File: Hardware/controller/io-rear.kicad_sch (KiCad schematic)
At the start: 7 parts

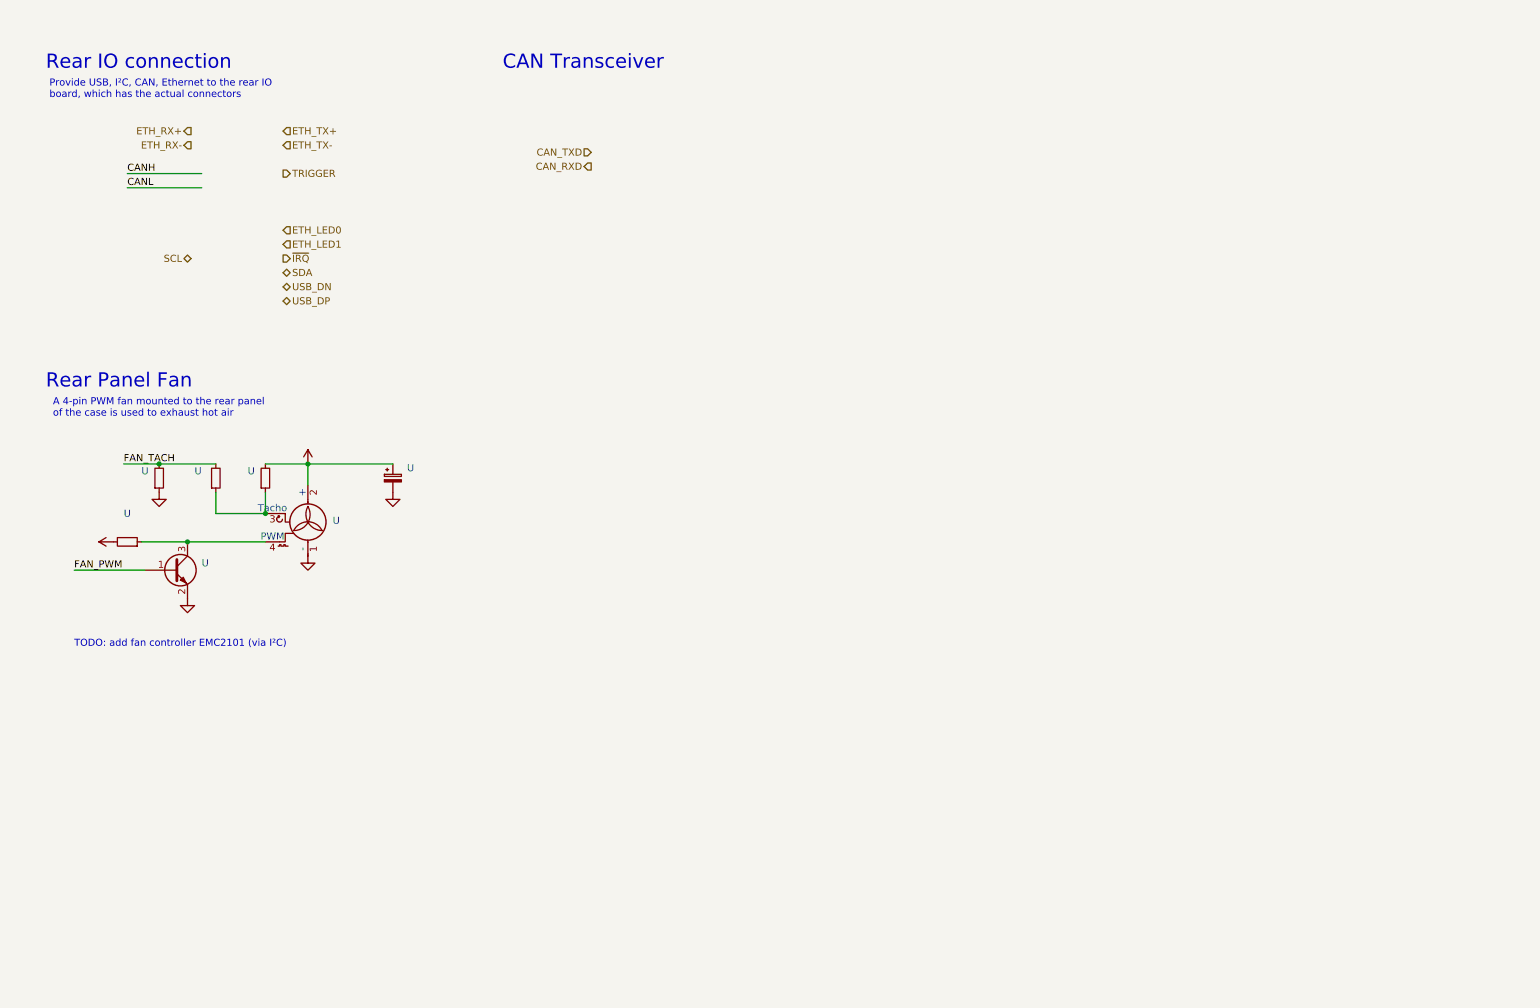
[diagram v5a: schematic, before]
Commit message: More reworking of the controller and friends
- Add more rear IO to the controller, in this case finishing positioning
  of the Ethernet jack, and adding a suitable right angle USB B jack
  (USB C is preferrable but there's basically no jacks that are
  sufficiently long)

- Mostly finish power section on controller (save for the enable input
  for our +3V3 rail; it'll be slaved off the SoM +3V3 rail)

- Minor tweaks to pinout of FFC connector on front panel

- Update cutout shape of analog board

- Fixed a few footprints metadata

- Add footprints for further rear panel IO
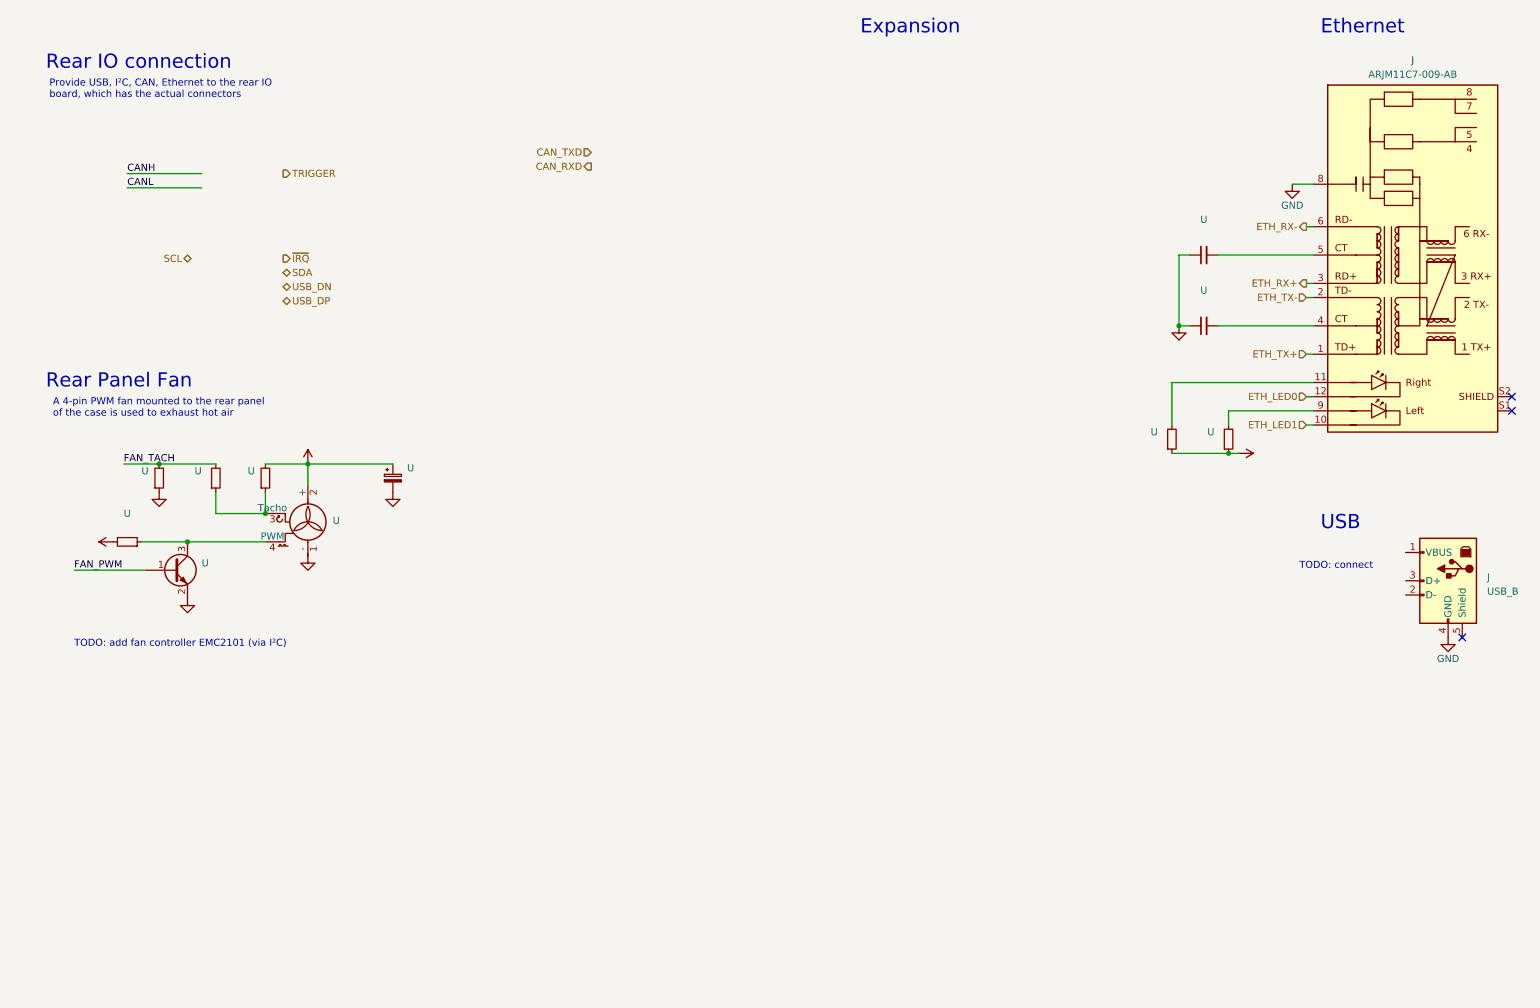
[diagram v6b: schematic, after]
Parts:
- added J: USB_B, symbol Connector:USB_B
- added J: ARJM11C7-009-AB, programmable-load:Abracon-ARJM11C7, symbol programmable-load:ARJM11C7-009-AB
- added U (x2): (no value), symbol Device:R_Small
- added U (x2): (no value), symbol Device:C_Small
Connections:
- net ETH_LED0: now also J.12 (LLED-)
- net ETH_LED1: now also J.10 (RLED-)
- net ETH_RX+: now also J.3 (RD+)
- net ETH_RX-: now also J.6 (RD-)
- net ETH_TX+: now also J.1 (TD+)
- net ETH_TX-: now also J.2 (TD-)
- net GND: now also J.4 (GND), J.8, U.1, U.1
- new net: J.9 (RLED+), U.2
- new net: J.11 (LLED+), U.2
- new net: J.5 (CT), U.2
- new net: J.4 (CT), U.2
- new net +3V3: U.1, U.1
- no-connect marks 0 -> 3
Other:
- note added: "Ethernet"
- note added: "Expansion"
- note added: "TODO: connect"
- note added: "USB"
- note removed: "CAN Transceiver"

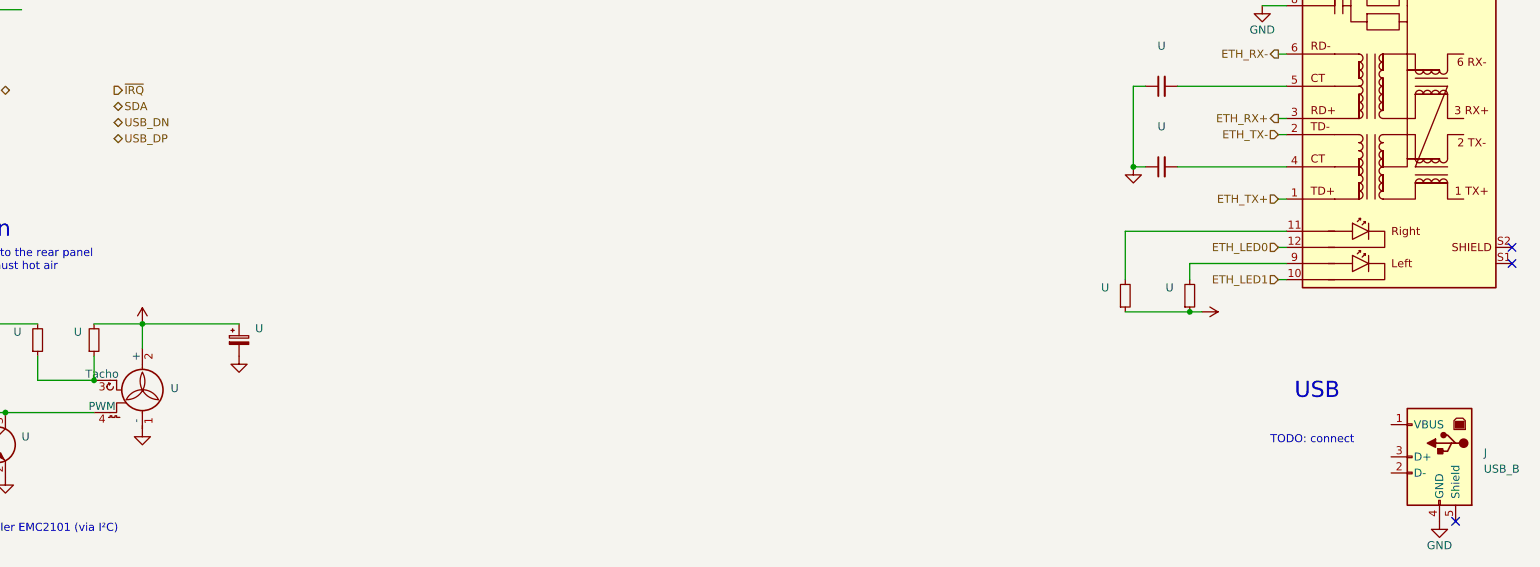
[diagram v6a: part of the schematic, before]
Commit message: More controller power supply work
- Added a voltage supervisor on the SoM's +3V3 rail, which disables our
  +3V3 switching regulator until the SoM rail has come up to a
  reasonable voltage. This avoids the +3V3 rail being powered, and back
  powering stuff on the SoM through ESD diodes.

  There's also a resistor (R204) that may or may not be needed to hold
  the regulator disabled until the power supervisor does its thing; this
  needs to be investigated

- Added ESD protection for USB device jack

- Tweaks to footprint for ARJM11C7 Ethernet jack, to fix DRC errors with
  the LED pads and the mechanical retention thingies
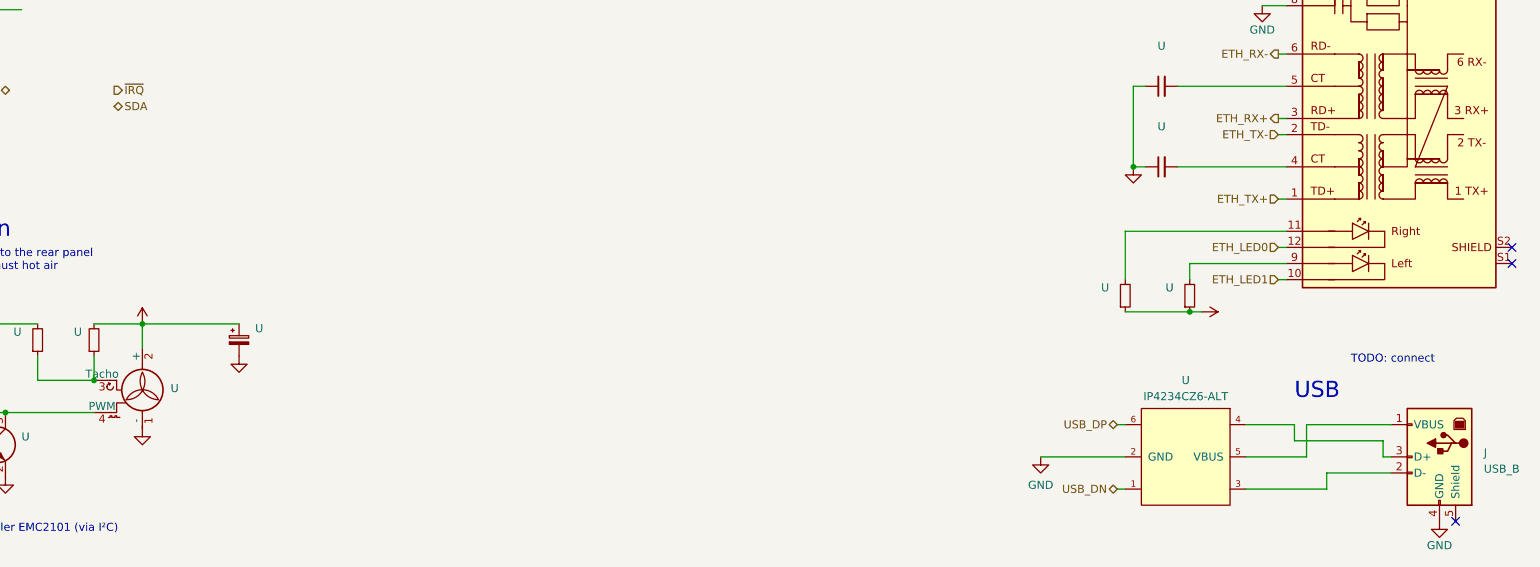
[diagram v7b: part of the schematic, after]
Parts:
- added U: IP4234CZ6-ALT, Package_SO:TSOP-6_1.65x3.05mm_P0.95mm, symbol programmable-load:IP4234CZ6-ALT
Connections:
- net GND: now also U.2 (GND)
- net USB_DN: now also U.1
- net USB_DP: now also U.6
- net at J.1 (VBUS): now also U.5 (VBUS)
- net at J.2 (D-): now also U.3
- net at J.3 (D+): now also U.4
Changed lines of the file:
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@@
+    (stroke (width 0) (type default))
+  )
+  (wire (pts (xy 219.71 121.92) (xy 220.98 121.92))
+    (stroke (width 0) (type default))
+  )
+  (wire (pts (xy 261.62 114.3) (xy 261.62 116.84))
     (stroke (width 0) (type default))
   )
@@
     (stroke (width 0) (type default))
   )
+  (wire (pts (xy 247.65 114.3) (xy 247.65 111.76))
+    (stroke (width 0) (type default))
+  )
   (wire (pts (xy 245.11 66.04) (xy 246.38 66.04))
     (stroke (width 0) (type default))
@@
     (stroke (width 0) (type default))
   )
+  (wire (pts (xy 249.555 111.76) (xy 262.89 111.76))
+    (stroke (width 0) (type default))
+  )
   (wire (pts (xy 49.53 104.775) (xy 49.53 100.965))
     (stroke (width 0) (type default))
   )
+  (wire (pts (xy 219.71 111.76) (xy 220.98 111.76))
+    (stroke (width 0) (type default))
+  )
   (wire (pts (xy 245.11 83.82) (xy 246.38 83.82))
     (stroke (width 0) (type default))
   )
+  (wire (pts (xy 207.645 116.84) (xy 220.98 116.84))
+    (stroke (width 0) (type default))
+  )
+  (wire (pts (xy 252.73 119.38) (xy 252.73 121.92))
+    (stroke (width 0) (type default))
+  )
   (wire (pts (xy 231.14 93.98) (xy 233.045 93.98))
     (stroke (width 0) (type default))
@@
     (stroke (width 0) (type default))
   )
+  (wire (pts (xy 247.65 111.76) (xy 240.03 111.76))
+    (stroke (width 0) (type default))
+  )
+  (wire (pts (xy 247.65 114.3) (xy 261.62 114.3))
+    (stroke (width 0) (type default))
+  )
   (wire (pts (xy 231.14 86.36) (xy 231.14 88.9))
     (stroke (width 0) (type default))
@@
     (stroke (width 0) (type default))
   )
+  (wire (pts (xy 262.89 119.38) (xy 252.73 119.38))
+    (stroke (width 0) (type default))
+  )
+  (wire (pts (xy 262.89 116.84) (xy 261.62 116.84))
+    (stroke (width 0) (type default))
+  )
   (wire (pts (xy 246.38 81.28) (xy 220.98 81.28))
     (stroke (width 0) (type default))
@@
     (stroke (width 0) (type default))
   )
+  (wire (pts (xy 252.73 121.92) (xy 240.03 121.92))
+    (stroke (width 0) (type default))
+  )
   (wire (pts (xy 242.57 45.72) (xy 246.38 45.72))
     (stroke (width 0) (type default))
@@
     (stroke (width 0) (type default))
   )
+  (wire (pts (xy 240.03 116.84) (xy 249.555 116.84))
+    (stroke (width 0) (type default))
+  )
   (wire (pts (xy 58.42 95.885) (xy 66.04 95.885))
     (stroke (width 0) (type default))
@@
   )
   (wire (pts (xy 222.25 58.42) (xy 224.155 58.42))
+    (stroke (width 0) (type default))
+  )
+  (wire (pts (xy 249.555 111.76) (xy 249.555 116.84))
     (stroke (width 0) (type default))
   )
@@
     (effects (font (size 2.54 2.54)) (justify left bottom))
   )
-  (text "TODO: connect" (at 243.84 114.935 0)
+  (text "TODO: connect" (at 256.54 102.235 0)
     (effects (font (size 1.27 1.27)) (justify left bottom))
   )
@@
     (effects (font (size 1.27 1.27)) (justify right))
   )
-  (hierarchical_label "USB_DN" (shape bidirectional) (at 61.595 64.135 0) (fields_autoplaced)
-    (effects (font (size 1.27 1.27)) (justify left))
+  (hierarchical_label "USB_DN" (shape bidirectional) (at 219.71 121.92 180) (fields_autoplaced)
+    (effects (font (size 1.27 1.27)) (justify right))
   )
   (hierarchical_label "SDA" (shape bidirectional) (at 61.595 61.595 0) (fields_autoplaced)
@@
     (effects (font (size 1.27 1.27)) (justify right))
   )
-  (hierarchical_label "USB_DP" (shape bidirectional) (at 61.595 66.675 0) (fields_autoplaced)
-    (effects (font (size 1.27 1.27)) (justify left))
+  (hierarchical_label "USB_DP" (shape bidirectional) (at 219.71 111.76 180) (fields_autoplaced)
+    (effects (font (size 1.27 1.27)) (justify right))
   )
   (hierarchical_label "ETH_LED1" (shape input) (at 245.11 88.9 180) (fields_autoplaced)
@@
     (effects (font (size 1.27 1.27)) (justify right))
   )
+  (symbol (lib_id "power:GND") (at 207.645 116.84 0) (unit 1)
+    (in_bom yes) (on_board yes)
+    (default_instance (reference "#PWR") (unit 1) (value "GND") (footprint ""))
+    (property "Reference" "#PWR" (id 0) (at 207.645 123.19 0)
+      (effects (font (size 1.27 1.27)) hide)
+    )
+    (property "Value" "GND" (id 1) (at 207.645 121.285 0)
+      (effects (font (size 1.27 1.27)))
+    )
+    (property "Footprint" "" (id 2) (at 207.645 116.84 0)
+      (effects (font (size 1.27 1.27)) hide)
+    )
+    (property "Datasheet" "" (id 3) (at 207.645 116.84 0)
+      (effects (font (size 1.27 1.27)) hide)
+    )
+    (pin "1")
+  )
+  (symbol (lib_id "programmable-load:IP4234CZ6-ALT") (at 237.49 109.22 0) (mirror y) (unit 1)
+    (in_bom yes) (on_board yes)
+    (default_instance (reference "U") (unit 1) (value "IP4234CZ6-ALT") (footprint "Package_SO:TSOP-6_1.65x3.05mm_P0.95mm"))
+    (property "Reference" "U" (id 0) (at 230.505 104.775 0)
+      (effects (font (size 1.27 1.27)))
+    )
+    (property "Value" "IP4234CZ6-ALT" (id 1) (at 230.505 107.315 0)
+      (effects (font (size 1.27 1.27)))
+    )
+    (property "Footprint" "Package_SO:TSOP-6_1.65x3.05mm_P0.95mm" (id 2) (at 237.49 86.36 0)
+      (effects (font (size 1.27 1.27)) (justify right) hide)
+    )
+    (property "Datasheet" "https://assets.nexperia.com/documents/data-sheet/IP4234CZ6.pdf" (id 3) (at 237.49 83.82 0)
+      (effects (font (size 1.27 1.27)) (justify right) hide)
+    )
+    (pin "1")
+    (pin "2")
+    (pin "3")
+    (pin "4")
+    (pin "5")
+    (pin "6")
+  )
   (symbol (lib_id "power:GND") (at 66.04 112.395 0) (unit 1)
